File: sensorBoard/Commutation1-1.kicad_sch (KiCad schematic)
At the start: 14 parts, among them Q10 2N7002, U20 BTS50080-1TEA

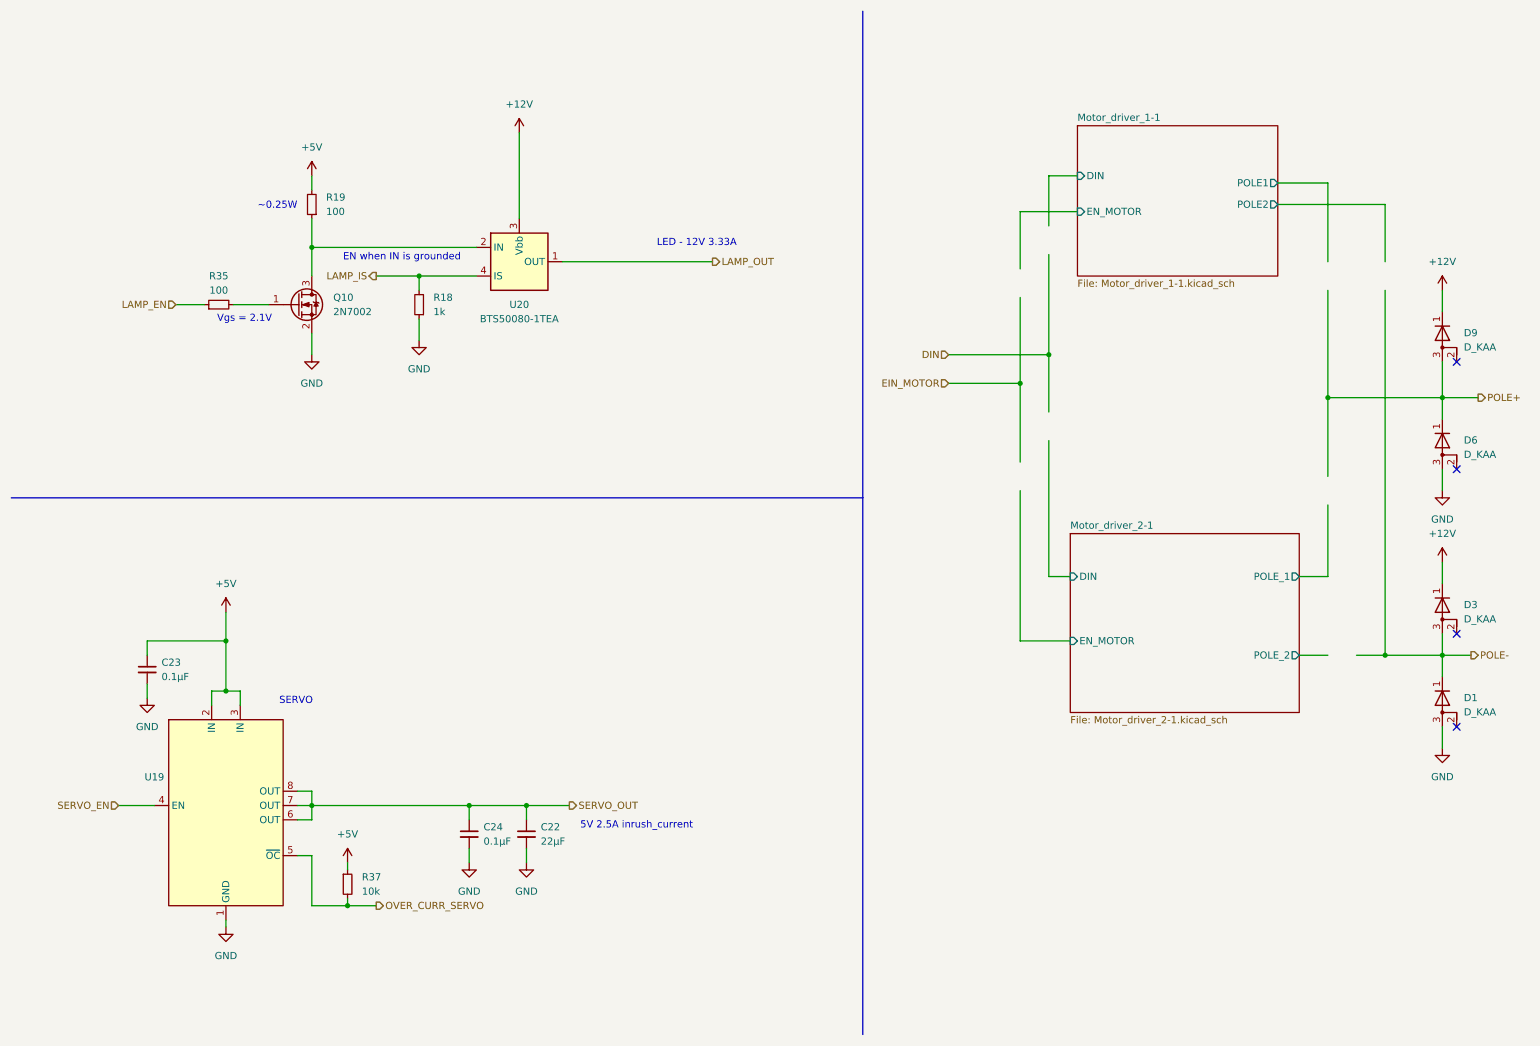
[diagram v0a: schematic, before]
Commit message: new two separate pcbs
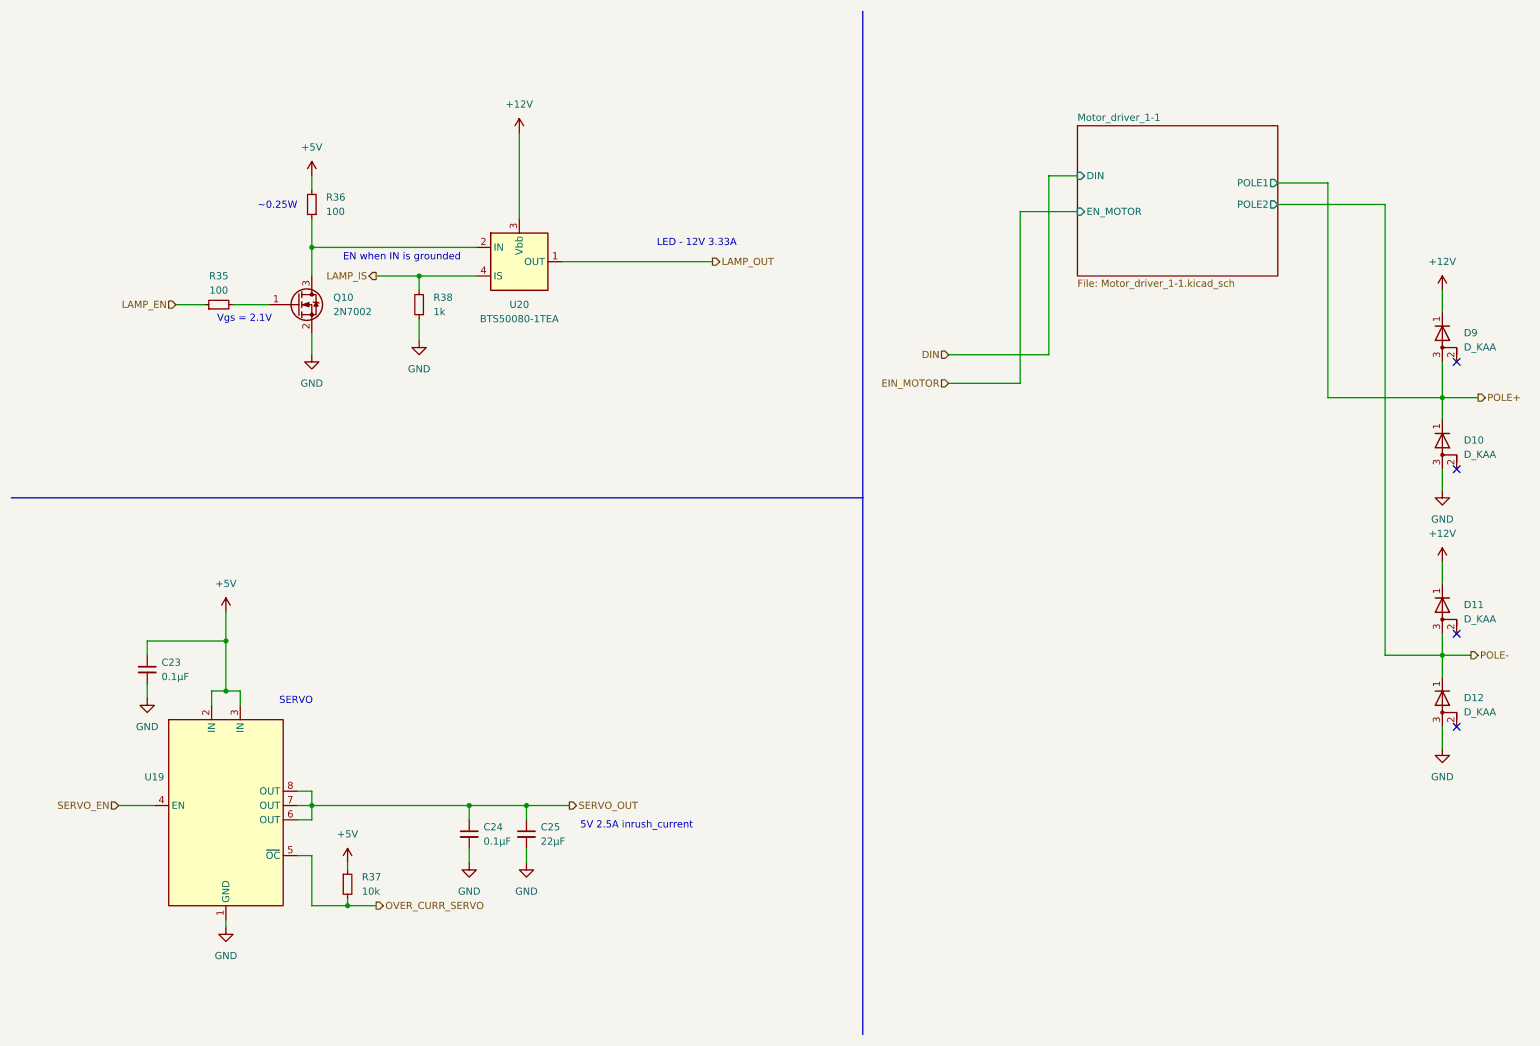
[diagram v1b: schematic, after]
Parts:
- renumbered C22 to C25, D6 to D10, D3 to D11, D1 to D12, R19 to R36, R18 to R38
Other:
- removed sheet Motor_driver_2-1

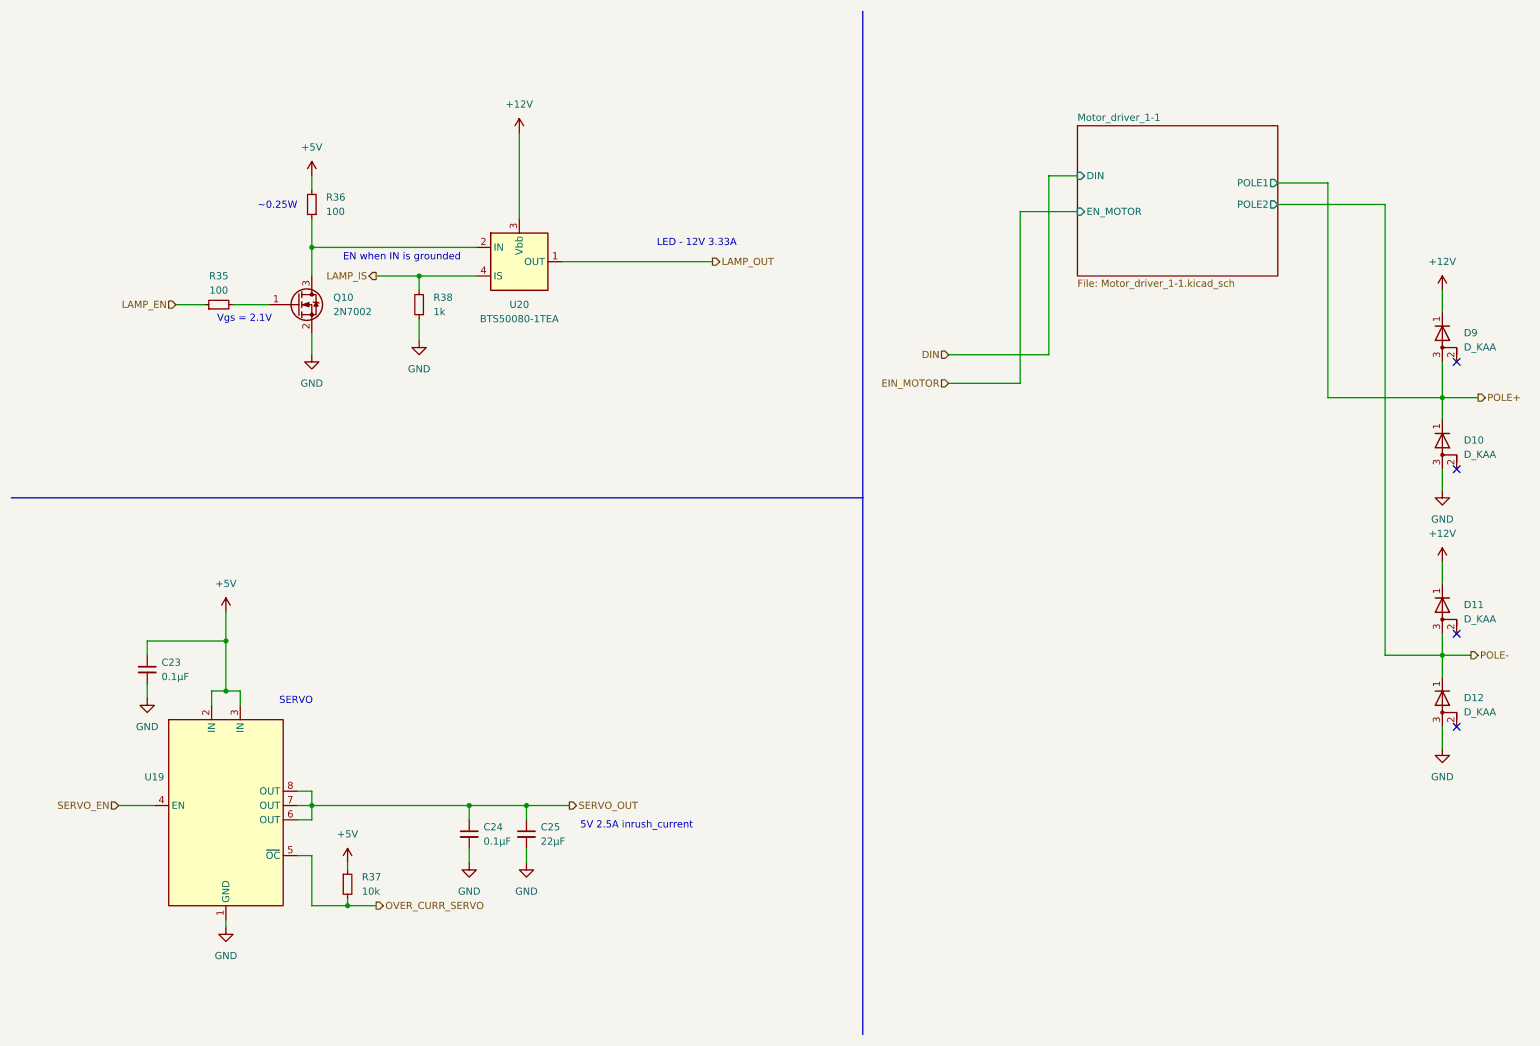
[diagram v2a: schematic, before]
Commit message: added old software + new PCB
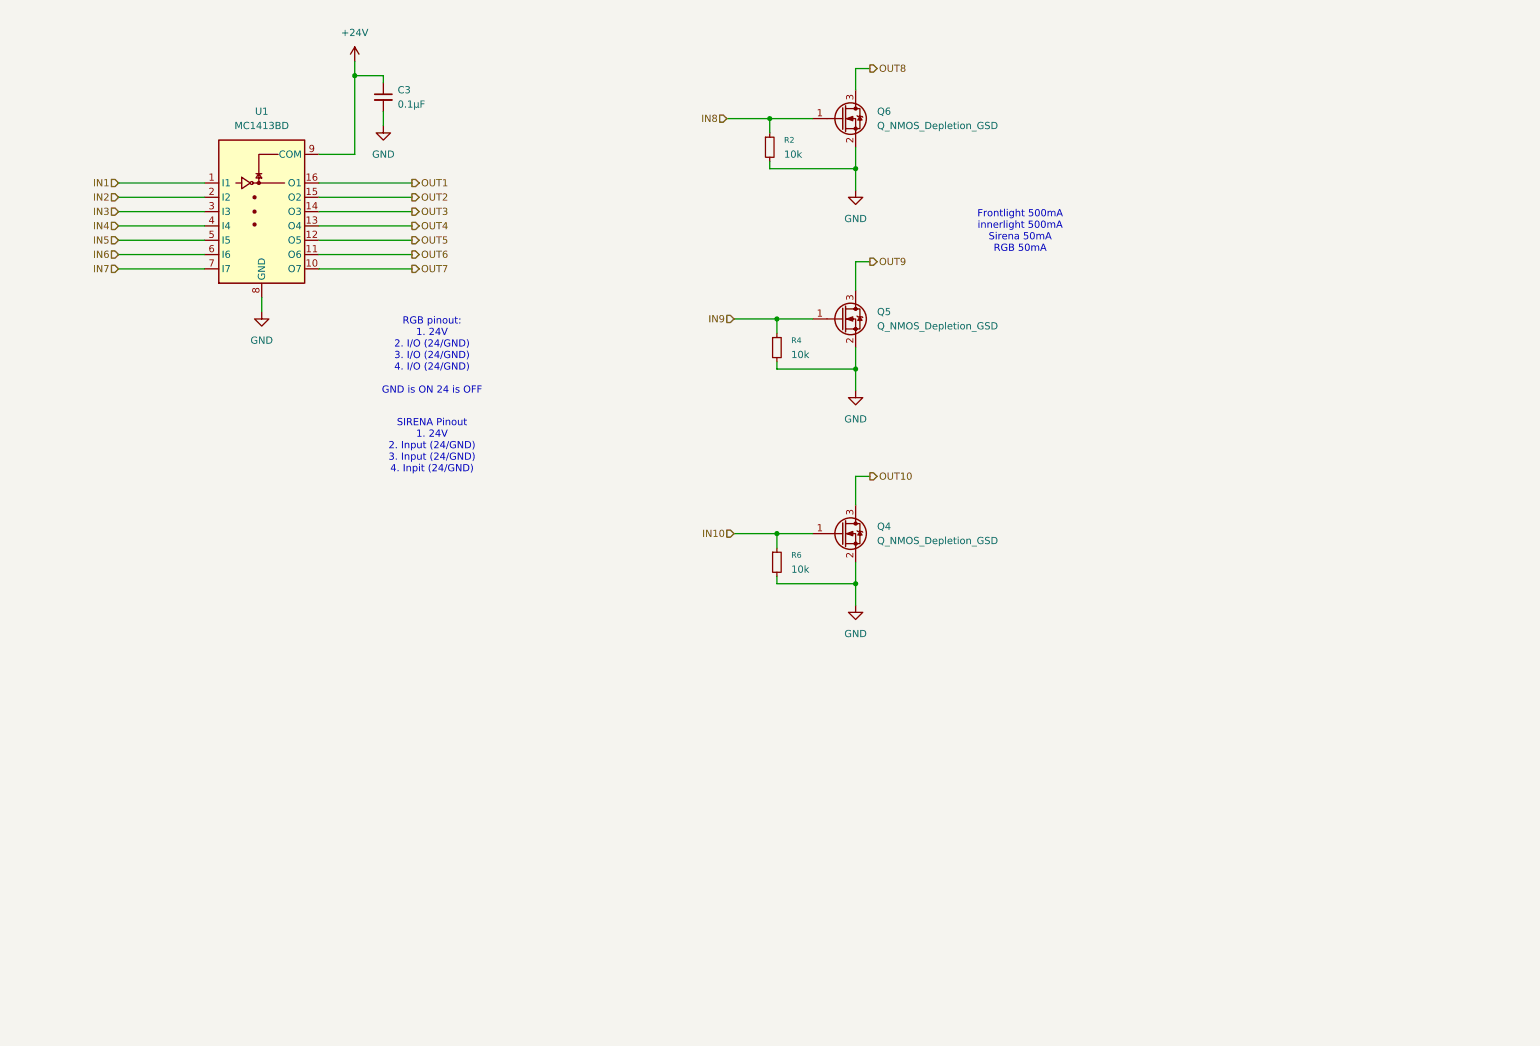
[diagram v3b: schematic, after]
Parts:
- removed C23, C24: 0.1µF, Capacitor_SMD:C_0805_2012Metric, symbol Device:C_Small
- removed C25: 22µF, Capacitor_SMD:C_0805_2012Metric, symbol Device:C_Small
- removed D10, D11, D12, D9: D_KAA, Package_TO_SOT_SMD:TO-277A, symbol Device:D_KAA
- removed Q10: 2N7002, Package_TO_SOT_SMD:SOT-23, symbol Transistor_FET:2N7002
- removed R35, R36: 100, Resistor_SMD:R_0805_2012Metric, symbol Device:R_Small
- removed R37: 10k, Resistor_SMD:R_0805_2012Metric, symbol Device:R_Small
- removed R38: 1k, Resistor_SMD:R_0805_2012Metric, symbol Device:R_Small
- removed U19: ~, Package_SO:SOIC-8_3.9x4.9mm_P1.27mm, symbol New_Library:TPS2034
- removed U20: BTS50080-1TEA, Package_TO_SOT_SMD:TO-252-4, symbol Power_Management:BTS50080-1TEA
- added C3: 0.1µF, Capacitor_SMD:C_0603_1608Metric, symbol Device:C_Small
- added Q4, Q5, Q6: Q_NMOS_Depletion_GSD, Package_TO_SOT_SMD:SOT-23, symbol Transistor_FET_Other:Q_NMOS_Depletion_GSD
- added R2, R4, R6: 10k, Resistor_SMD:R_0805_2012Metric, symbol Device:R_Small
- added U1: MC1413BD, Package_SO:SOIC-16_3.9x9.9mm_P1.27mm, symbol Transistor_Array:MC1413BD
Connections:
- net GND: now also C3.2, Q4.2 (S), Q5.2 (S), Q6.2 (S), R2.2, R4.2, R6.2, U1.8 (GND)
- new net +24V: C3.1, U1.9 (COM)
- new net IN1: U1.1 (I1)
- new net IN10: Q4.1 (G), R6.1
- new net IN2: U1.2 (I2)
- new net IN3: U1.3 (I3)
- new net IN4: U1.4 (I4)
- new net IN5: U1.5 (I5)
- new net IN6: U1.6 (I6)
- new net IN7: U1.7 (I7)
- new net IN8: Q6.1 (G), R2.1
- new net IN9: Q5.1 (G), R4.1
- new net OUT1: U1.16 (O1)
- new net OUT10: Q4.3 (D)
- new net OUT2: U1.15 (O2)
- new net OUT3: U1.14 (O3)
- new net OUT4: U1.13 (O4)
- new net OUT5: U1.12 (O5)
- new net OUT6: U1.11 (O6)
- new net OUT7: U1.10 (O7)
- new net OUT8: Q6.3 (D)
- new net OUT9: Q5.3 (D)
- no-connect marks 4 -> 0
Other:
- removed sheet Motor_driver_1-1
- note added: "Frontlight 500mA innerlight 500mA Sirena 50mA RGB 50mA"
- note added: "RGB pinout: 1. 24V 2. I/O (24/GND) 3. I/O (24/GND) 4. I/O (24/GND) GND is ON 24 is OFF"
- note added: "SIRENA Pinout 1. 24V 2. Input (24/GND) 3. Input (24/GND) 4. Inpit (24/GND)"
- note removed: "5V 2.5A inrush_current"
- note removed: "EN when IN is grounded"
- note removed: "LED - 12V 3.33A"
- note removed: "SERVO"
- note removed: "Vgs = 2.1V"
- note removed: "~0.25W"
